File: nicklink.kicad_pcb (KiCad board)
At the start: 2 copper layers, 34 x 33 mm, 34 parts, among them J1 Conn_02x10_Odd_Even, J2 USB_C_Receptacle_USB2.0_16P, J3 Conn_02x10_Odd_Even, SW1 SW_SPDT, U1 STM32F103C8T6, U2 AMS1117-3.3, Y1 16MHz

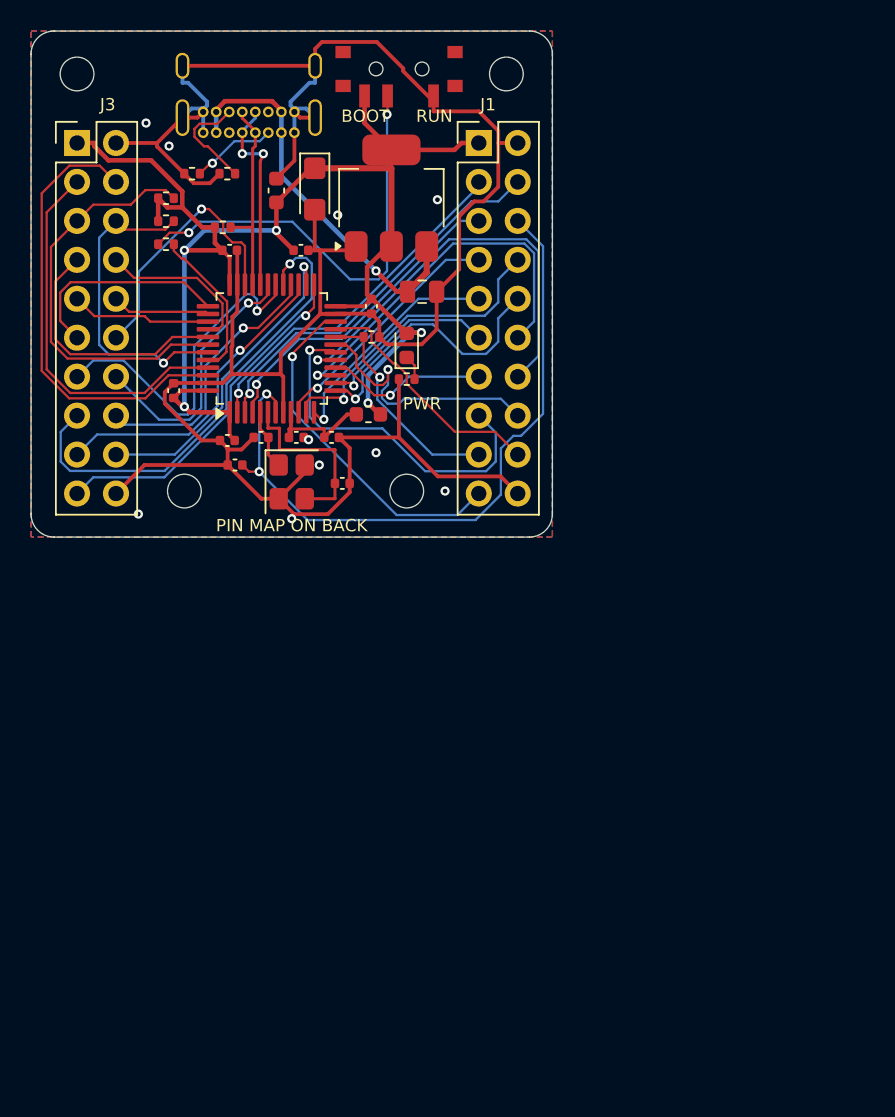
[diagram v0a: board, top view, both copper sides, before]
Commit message: NickLink v1.2 — smaller board, front pin labels, QoL fixes
Board shrinks from 34 x 33 mm to 33.19 x 25.5 mm (-25% area) while keeping
both 2x10 headers and all four M2 holes, and every header pin is now labelled
beside it on the front silkscreen.

Hardware changes:
- 5 V on J1.1 (USB VBUS via 1N5819WS Schottky; usable as a <=5.5 V input)
- RESET and BOOT buttons (B3U); NRST moved to J3 next to SWDIO/SWCLK/SWO
- 8 MHz HSE crystal (was 16 MHz), 15 pF load caps
- TLV75533 WSON LDO + ceramics replaces AMS1117 + tantalum
- USBLC6-2P6 ESD on D+/D-/VBUS
- I2C pull-ups on PB6/PB7 removed; user LED on PC13
- Header pinout reordered to follow the MCU package order

The design is now generated: tools/spec.py and tools/placement.py drive the
schematic, placement, Freerouting autoroute, GND stitching, DRC and fab
outputs (tools/build_all.sh, tools/fab.sh), all in Docker. ERC 0/0, DRC 0
violations / 0 unconnected / 0 parity issues.

Docs, renders, pinout CSV, schematic PDF, assembly/copper PDFs and
fabrication/v1.2 (Gerbers, drills, JLC BOM/CPL) are updated; v1.1 fab
outputs are kept.

Co-Authored-By: Claude Opus 5.5 <noreply@anthropic.com>
Claude-Session: https://claude.ai/code/session_01KPMtzubqGeBFaq48UcVZaf
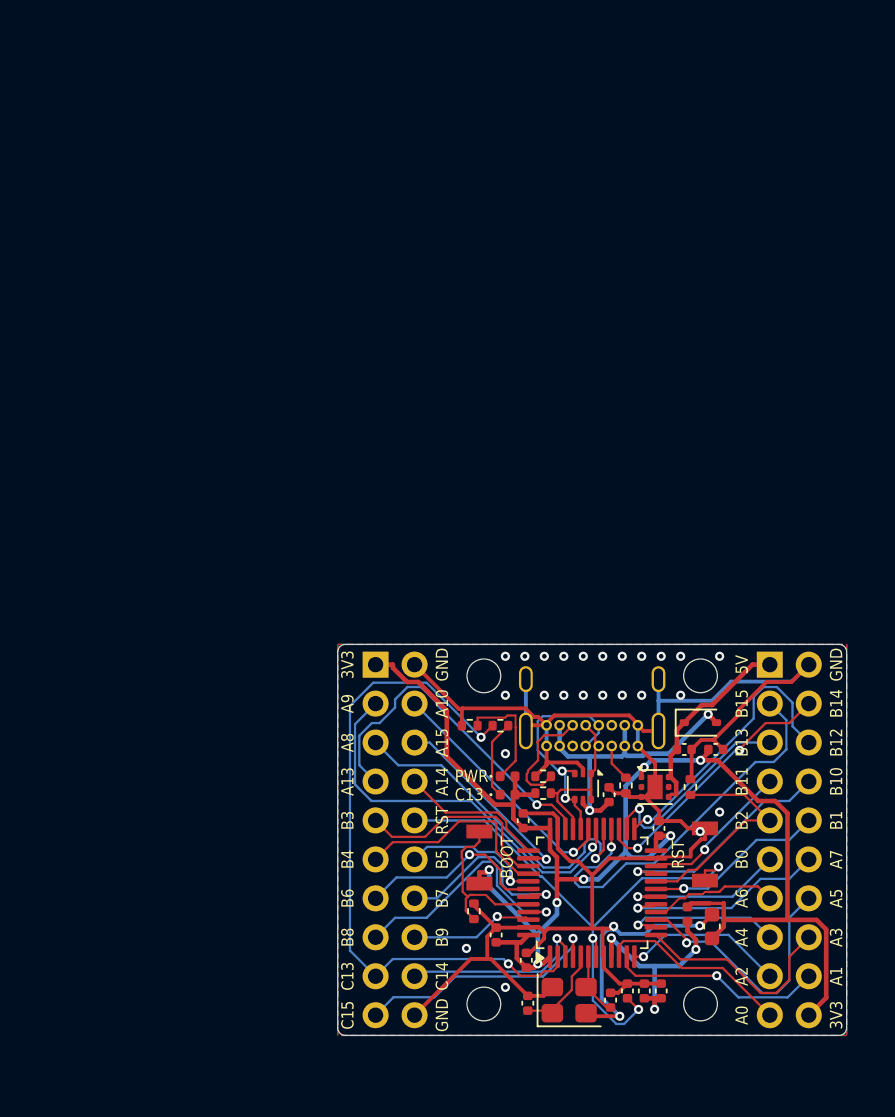
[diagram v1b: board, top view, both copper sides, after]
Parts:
- removed R7: 1k5, Resistor_SMD:R_0402_1005Metric
- added D2: 1N5819WS, Diode_SMD:D_SOD-323, F.Cu at (123.7, 105.1)
- added D3: GREEN, LED_SMD:LED_0402_1005Metric, F.Cu at (111.1, 109.8)
- added SW2: BOOT0, nicklink:SW_SPST_B3U-1000P_NoSilk, F.Cu at (109.2, 113.9)
- added U3: USBLC6-2P6, Package_TO_SOT_SMD:SOT-666, F.Cu at (116.0, 109.3)
- C10, C11: value 10p -> 15p
- C12: value 4.7u -> 1u; footprint Capacitor_SMD:C_0805_2012Metric -> Capacitor_SMD:C_0402_1005Metric
- C13: value 22u tantalum -> 100n; footprint Capacitor_Tantalum_SMD:CP_EIA-3216-18_Kemet-A -> Capacitor_SMD:C_0402_1005Metric
- D1: footprint LED_SMD:LED_0603_1608Metric -> LED_SMD:LED_0402_1005Metric
- FB1: value 120R -> 120R@100MHz; footprint Inductor_SMD:L_0603_1608Metric -> Inductor_SMD:L_0402_1005Metric
- H1: value MountingHole_2.2mm_M2 -> H1; footprint MountingHole_2.2mm_M2 -> MountingHole:MountingHole_2.2mm_M2_ISO7380
- H2: value MountingHole_2.2mm_M2 -> H2; footprint MountingHole_2.2mm_M2 -> MountingHole:MountingHole_2.2mm_M2_ISO7380
- H3: value MountingHole_2.2mm_M2 -> H3; footprint MountingHole_2.2mm_M2 -> MountingHole:MountingHole_2.2mm_M2_ISO7380
- H4: value MountingHole_2.2mm_M2 -> H4; footprint MountingHole_2.2mm_M2 -> MountingHole:MountingHole_2.2mm_M2_ISO7380
- J1, J3: footprint Connector_PinHeader_2.54mm:PinHeader_2x10_P2.54mm_Vertical -> nicklink:PinHeader_2x10_P2.54mm_Vertical_NoSilk
- SW1: value SW_SPDT -> RESET; footprint nicklink:SW_SPDT_PCM12_EdgeSilk -> nicklink:SW_SPST_B3U-1000P_NoSilk
- U2: value AMS1117-3.3 -> TLV75533PDRV; footprint Package_TO_SOT_SMD:SOT-223-3_TabPin2 -> Package_SON:WSON-6-1EP_2x2mm_P0.65mm_EP1x1.6mm
- Y1: value 16MHz -> 8MHz
- moved C5 55.8 mm to (124.4, 118.4)
- moved SW1 54.7 mm to (124.0, 113.7), turned to 90 degrees
- moved R4 48.9 mm to (118.8, 109.2), turned to 90 degrees
- moved R1 47.9 mm to (108.9, 117.4), turned to 90 degrees
- moved H1 47.4 mm to (109.5, 102.0)
- moved J2 45.8 mm to (119.6, 106.6)
- moved R5 44.4 mm to (113.4, 108.6)
- moved C13 43.9 mm to (117.7, 109.8), turned to 90 degrees
- moved C9 42.8 mm to (118.9, 122.6), turned to 90 degrees
- moved C6 42.6 mm to (120.0, 122.6), turned to 90 degrees
- moved C2 42.6 mm to (121.0, 112.0)
- moved R2 42.4 mm to (113.4, 109.7)
- moved C8 42.3 mm to (124.7, 106.8)
- moved U2 42.1 mm to (120.7, 109.3), turned to 0 degrees
- moved C7 42.0 mm to (121.1, 122.6), turned to 90 degrees
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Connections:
- net /SPI1_MISO renamed /PA6
- C12 pad 1: VBUS -> +5V
- C13 pad 1: +3.3V -> VBUS
- J1 pad 1: +3.3V -> +5V
- J1 pad 10: /PA3 -> /PB1
- J1 pad 11: /PA4 -> /PB0
- J1 pad 12: /SPI1_SCK -> /PA7
- J1 pad 14: /SPI1_MOSI -> /PA5
- J1 pad 15: /PB0 -> /PA4
- J1 pad 16: /PB1 -> /PA3
- J1 pad 17: /PB2 -> /PA2
- J1 pad 18: /PB10 -> /PA1
- J1 pad 19: /PB11 -> /PA0
- J1 pad 20: GND -> +3.3V
- J1 pad 3: /PC13 -> /PB15
- J1 pad 4: /PC14 -> /PB14
- J1 pad 5: /PC15 -> /PB13
- J1 pad 6: /NRST -> /PB12
- J1 pad 7: /PA0 -> /PB11
- J1 pad 8: /PA1 -> /PB10
- J1 pad 9: /PA2 -> /PB2
- J3 pad 10: /PA15 -> /NRST
- J3 pad 11: /SWCLK -> /PB4
- J3 pad 12: /SWDIO -> /PB5
- J3 pad 13: /USART1_TX -> /PB6
- J3 pad 14: /USART1_RX -> /PB7
- J3 pad 15: /PA8 -> /PB8
- J3 pad 16: /PB15 -> /PB9
- J3 pad 17: /PB14 -> /PC13
- J3 pad 18: /PB13 -> /PC14
- J3 pad 19: /PB12 -> /PC15
- J3 pad 3: /CAN_RX -> /PA9
- J3 pad 4: /CAN_TX -> /PA10
- J3 pad 5: /I2C1_SCL -> /PA8
- J3 pad 6: /I2C1_SDA -> /PA15
- J3 pad 7: /PB5 -> /PA13
- J3 pad 8: /PB4 -> /PA14
- R1 pad 1: /BOOT_SELECT -> /BOOT0
- R1 pad 2: /BOOT0 -> GND
- R6 pad 1: +3.3V -> /PC13
- R6 pad 2: /I2C1_SCL -> /USER_LED_K
- SW1 pad 1: GND -> /NRST
- SW1 pad 2: /BOOT_SELECT -> GND
- U1 pad 15: /SPI1_SCK -> /PA5
- U1 pad 17: /SPI1_MOSI -> /PA7
- U1 pad 30: /USART1_TX -> /PA9
- U1 pad 31: /USART1_RX -> /PA10
- U1 pad 34: /SWDIO -> /PA13
- U1 pad 37: /SWCLK -> /PA14
- U1 pad 42: /I2C1_SCL -> /PB6
- U1 pad 43: /I2C1_SDA -> /PB7
- U1 pad 45: /CAN_RX -> /PB8
- U1 pad 46: /CAN_TX -> /PB9
- U2 pad 1: GND -> +3.3V
- U2 pad 2: +3.3V -> unconnected-(U2-NC-Pad2)
- U2 pad 3: VBUS -> GND
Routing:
- net /CAN_TX: track 29.8 -> 0.00 mm
- net /BOOT_SELECT: track 28.7 -> 0.00 mm, vias 2 -> 0
- net /SPI1_MOSI: track 27.9 -> 0.00 mm, vias 1 -> 0
- net /I2C1_SCL: track 27.0 -> 0.00 mm
- net /PA9: track 0.00 -> 25.8 mm, vias 0 -> 1
- net /SPI1_SCK: track 25.1 -> 0.00 mm, vias 1 -> 0
- net /CAN_RX: track 24.9 -> 0.00 mm
- net GND: track 166.0 -> 141.7 mm, vias 10 -> 27
- net /PA13: track 0.00 -> 22.8 mm, vias 0 -> 1
- net /USART1_TX: track 22.5 -> 0.00 mm, vias 1 -> 0
- net /I2C1_SDA: track 20.6 -> 0.00 mm, vias 1 -> 0
- net /PC13: track 23.2 -> 43.7 mm, vias 1 -> 2
- net /SWDIO: track 17.4 -> 0.00 mm, vias 1 -> 0
- net /USART1_RX: track 17.3 -> 0.00 mm, vias 1 -> 0
- net /PA5: track 0.00 -> 17.1 mm, vias 0 -> 1
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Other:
- board size 34 x 33 mm -> 33.2 x 25.5 mm
- board text added: "3V3 out: 250 mA max"
- board text added: "5V"
- board text added: "5V: USB out/<=5.5V in"
- board text added: "A0"
- board text added: "A1"
- board text added: "A10"
- board text added: "A13"
- board text added: "A13 SWDIO A14 SWCLK"
- board text added: "A14"
- board text added: "A15"
- board text added: "A2"
- board text added: "A3"
- board text added: "A4"
- board text added: "A5"
- board text added: "A5 SCK1 A6 MISO1"
- board text added: "A6"
- board text added: "A7"
- board text added: "A7 MOSI1 B2 BOOT1"
- board text added: "A8"
- board text added: "A9"
- board text added: "A9 TX1 A10 RX1"
- board text added: "B0"
- board text added: "B1"
- board text added: "B10"
- board text added: "B11"
- board text added: "B12"
- board text added: "B13"
- board text added: "B14"
- board text added: "B15"
- board text added: "B2"
- board text added: "B3"
- board text added: "B3 SWO RST NRST"
- board text added: "B4"
- board text added: "B5"
- board text added: "B6"
- board text added: "B6 SCL1 B7 SDA1"
- board text added: "B7"
- board text added: "B8"
- board text added: "B8 CANRX B9 CANTX"
- board text added: "B9"
- board text added: "C13"
- board text added: "C13 LED (low=on)"
- board text added: "C14"
- board text added: "C15"
- board text added: "NickLink v1.2"
- board text added: "RST"
- board text added: "STM32F103C8 8MHz"
- board text removed: "01"
- board text removed: "02"
- board text removed: "03"
- board text removed: "04"
- board text removed: "05"
- board text removed: "06"
- board text removed: "07"
- board text removed: "08"
- board text removed: "09"
- board text removed: "10"
- board text removed: "11"
- board text removed: "12"
- board text removed: "13"
- board text removed: "14"
- board text removed: "15"
- board text removed: "16"
- board text removed: "17"
- board text removed: "18"
- board text removed: "19"
- board text removed: "20"
- board text removed: "J1"
- board text removed: "J1 PINOUT"
- board text removed: "J3"
- board text removed: "J3 PINOUT"
- board text removed: "NRST"
- board text removed: "NickLink v1.1"
- board text removed: "PA0"
- board text removed: "PA1"
- board text removed: "PA10"
- board text removed: "PA13"
- board text removed: "PA14"
- board text removed: "PA15"
- board text removed: "PA2"
- board text removed: "PA3"
- board text removed: "PA4"
- board text removed: "PA5"
- board text removed: "PA6"
- board text removed: "PA7"
- board text removed: "PA8"
- board text removed: "PA9"
- board text removed: "PB0"
- board text removed: "PB1"
- board text removed: "PB10"
- board text removed: "PB11"
- board text removed: "PB12"
- board text removed: "PB13"
- board text removed: "PB14"
- board text removed: "PB15"
- board text removed: "PB2"
- board text removed: "PB3"
- board text removed: "PB4"
- board text removed: "PB5"
- board text removed: "PB6"
- board text removed: "PB7"
- board text removed: "PB8"
- board text removed: "PB9"
- board text removed: "PC13"
- board text removed: "PC14"
- board text removed: "PC15"
- board text removed: "PIN MAP ON BACK"
- board text removed: "RUN"
- board text removed: "STM32F103C8"

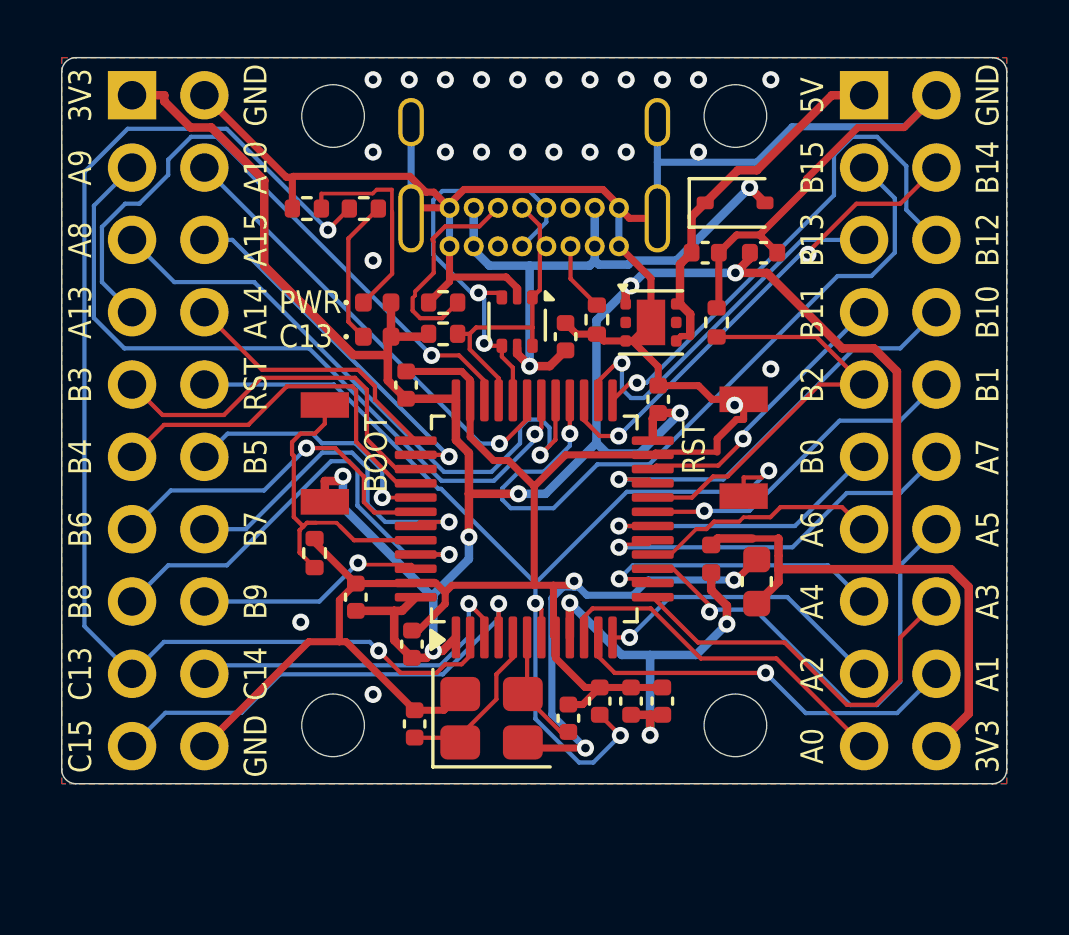
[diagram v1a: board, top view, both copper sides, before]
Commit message: NickLink v1.3 — on-board 6-axis IMU (LSM6DSV16X)
Adds an ST LSM6DSV16X accel+gyro on I2C1 (PB6/PB7, address 0x6A) with
INT1 on PA0 (WKUP), for motion tracking, robotics and tap-to-wake use.
Placed on the top side (single-sided assembly): the board grows to
33.19 x 28.8 mm (956 mm^2, still -15% vs v1.1). Pinout unchanged from v1.2.

- 4.7k I2C1 pull-ups restored (on-board device on the bus)
- Project symbol nicklink:LSM6DSV16X; top-copper keep-out under the package
- Crystal nets pre-routed as locked top-layer tracks (no vias)
- USBLC6 channels swapped so D+/D- don't cross at the MCU
- Min track width 0.10 mm to accept Freerouting neck-downs
- build_pcb.py --resilk for silkscreen-only edits; build_all.sh retries
  autoroute; seeded placement search documented in tools/README.md
- README, design review, pinout CSV, schematic, PDFs, renders, checks and
  fabrication/v1.3 updated

ERC 0/0; DRC 0 violations, 0 unconnected, 0 parity issues.

Co-Authored-By: Claude Opus 5.5 <noreply@anthropic.com>
Claude-Session: https://claude.ai/code/session_01KPMtzubqGeBFaq48UcVZaf
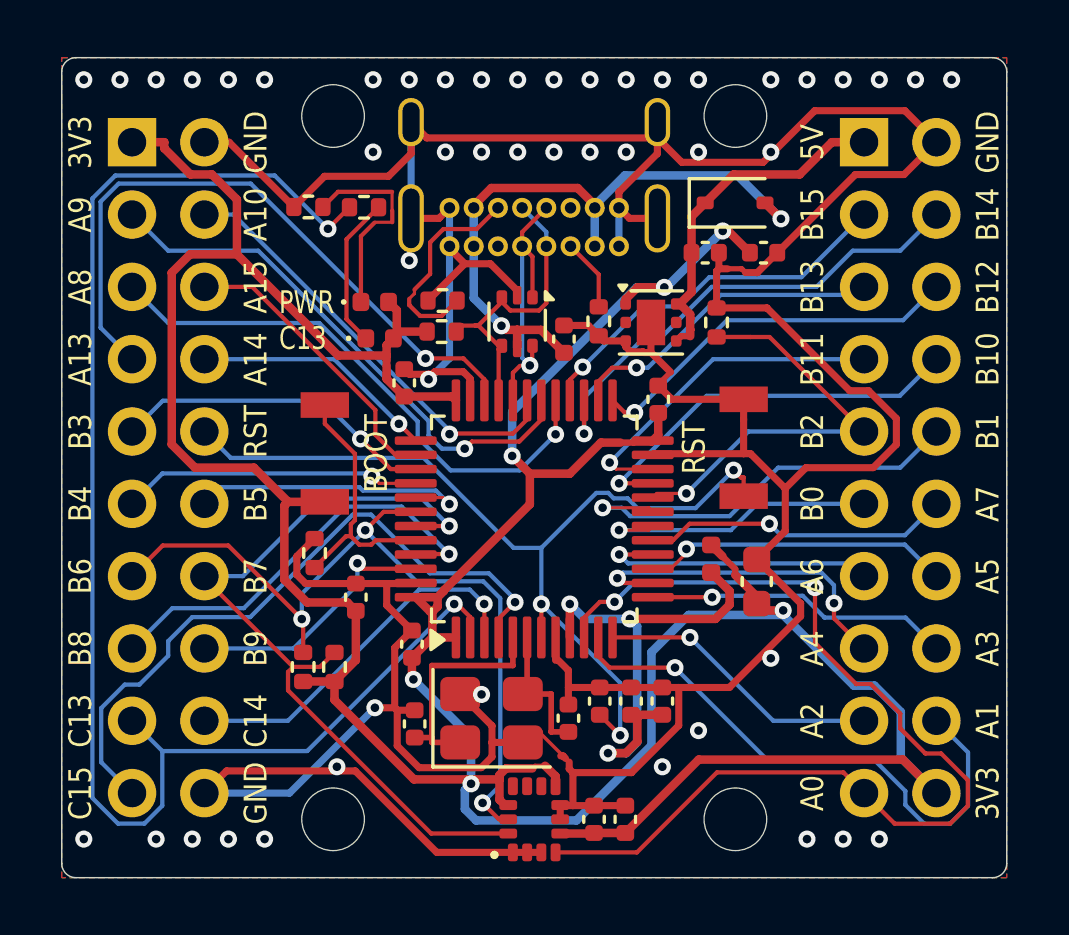
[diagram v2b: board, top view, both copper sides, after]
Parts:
- added C14: 100n, Capacitor_SMD:C_0402_1005Metric, F.Cu at (118.7, 126.8)
- added C15: 100n, Capacitor_SMD:C_0402_1005Metric, F.Cu at (119.8, 126.8)
- added R7: 4k7, Resistor_SMD:R_0402_1005Metric, F.Cu at (108.5, 121.4)
- added R9: 4k7, Resistor_SMD:R_0402_1005Metric, F.Cu at (109.6, 121.4)
- added U4: LSM6DSV16X, nicklink:LGA-14_3x2.5mm_P0.5mm_LayoutBorder3x4y_NoSilk, F.Cu at (116.6, 126.8)
- moved H3 3.30 mm to (109.5, 126.8)
- moved H4 3.30 mm to (123.7, 126.8)
- moved J1 1.65 mm to (128.2, 103.0)
- moved J3 1.65 mm to (102.5, 103.0)
- moved D3 0.10 mm to (111.2, 109.9)
- moved C13 0.10 mm to (117.6, 109.9)
- moved C3 0.10 mm to (112.0, 111.4)
- moved R2 0.10 mm to (113.3, 109.6)
- moved R4 0.09 mm to (118.9, 109.3)
- moved D1 0.09 mm to (111.0, 108.6)
- moved R3 0.08 mm to (108.7, 105.2)
- moved R5 0.07 mm to (113.4, 108.5)
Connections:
- U3 pad 1: /USB_D+ -> /USB_D-
- U3 pad 3: /USB_D- -> /USB_D+
- U3 pad 4: /USB_D- -> /USB_D+
- U3 pad 6: /USB_D+ -> /USB_D-
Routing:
- net +3.3V: track 98.4 -> 137.3 mm, vias 7 -> 6
- net GND: track 141.7 -> 169.3 mm, vias 27 -> 47
- net /PA0: track 12.7 -> 36.6 mm, vias 0 -> 2
- net /PB6: track 12.6 -> 29.1 mm, vias 1 -> 3
- net /PB7: track 12.7 -> 28.2 mm
- net /PB15: track 26.0 -> 13.5 mm
- net /PC13: track 43.7 -> 51.9 mm
- net /PC15: track 16.4 -> 23.9 mm
- net /PA9: track 25.8 -> 19.2 mm
- net /PA5: track 17.1 -> 10.9 mm
- net /PA1: track 13.9 -> 20.1 mm
- net /USB_D-: track 15.6 -> 10.4 mm, vias 2 -> 1
- net /PB12: track 18.4 -> 13.4 mm
- net /NRST: track 37.1 -> 32.9 mm
- net /PA3: track 13.9 -> 10.7 mm, vias 0 -> 1
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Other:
- board size 33.2 x 25.5 mm -> 33.2 x 28.8 mm
- board text added: "I2C1 B6/B7, INT1 A0"
- board text added: "IMU LSM6DSV16X 0x6A"
- board text added: "NickLink v1.3"
- board text removed: "NickLink v1.2"
